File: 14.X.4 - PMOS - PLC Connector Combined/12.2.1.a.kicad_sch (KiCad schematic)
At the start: 65 parts, among them J301 Conn_01x01_PAD, J302 Conn_01x01_PAD, J303 Conn_01x01_PAD, J304 Conn_01x01_PAD, J305 Conn_01x01_PAD, J306 Conn_01x01_PAD, J307 Conn_01x01_PAD, J308 Conn_01x01_PAD, J309 Conn_01x01_PAD, J310 Conn_01x01_PAD, J311 Conn_01x01_PAD, J312 Conn_01x01_PAD, J313 Conn_01x01_PAD, J314 Conn_01x01_PAD, J315 Conn_01x01_PAD, J316 Conn_01x01_PAD, J317 DB128L-5.08-2P-BK-S, J318 DB128L-5.08-3P-BK-S, J319 DB128L-5.08-2P-BK-S, J320 DB128L-5.08-2P-BK-S, J321 B04B-XASK-1, Q1 2N7002, Q2 2N7002, Q3 2N7002, Q4 2N7002, U1 DMP6023LE-13, U2 DMP6023LE-13, U3 DMP6023LE-13, U4 DMP6023LE-13

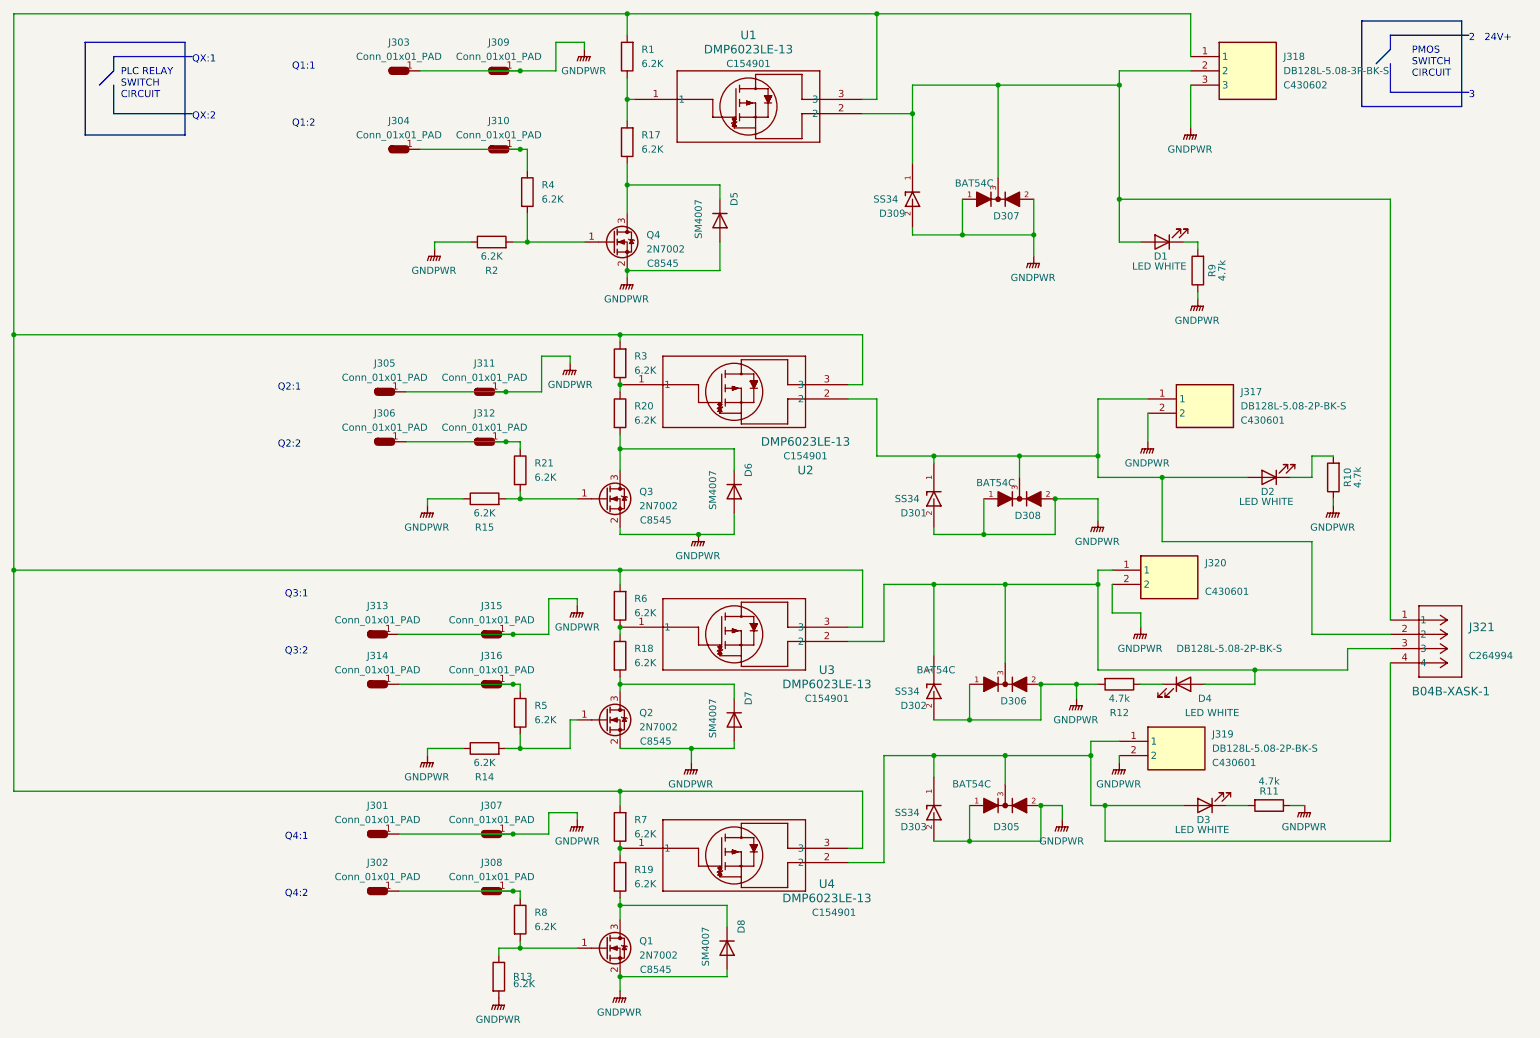
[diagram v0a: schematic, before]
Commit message: orientation of U1,U2,U3 and U4
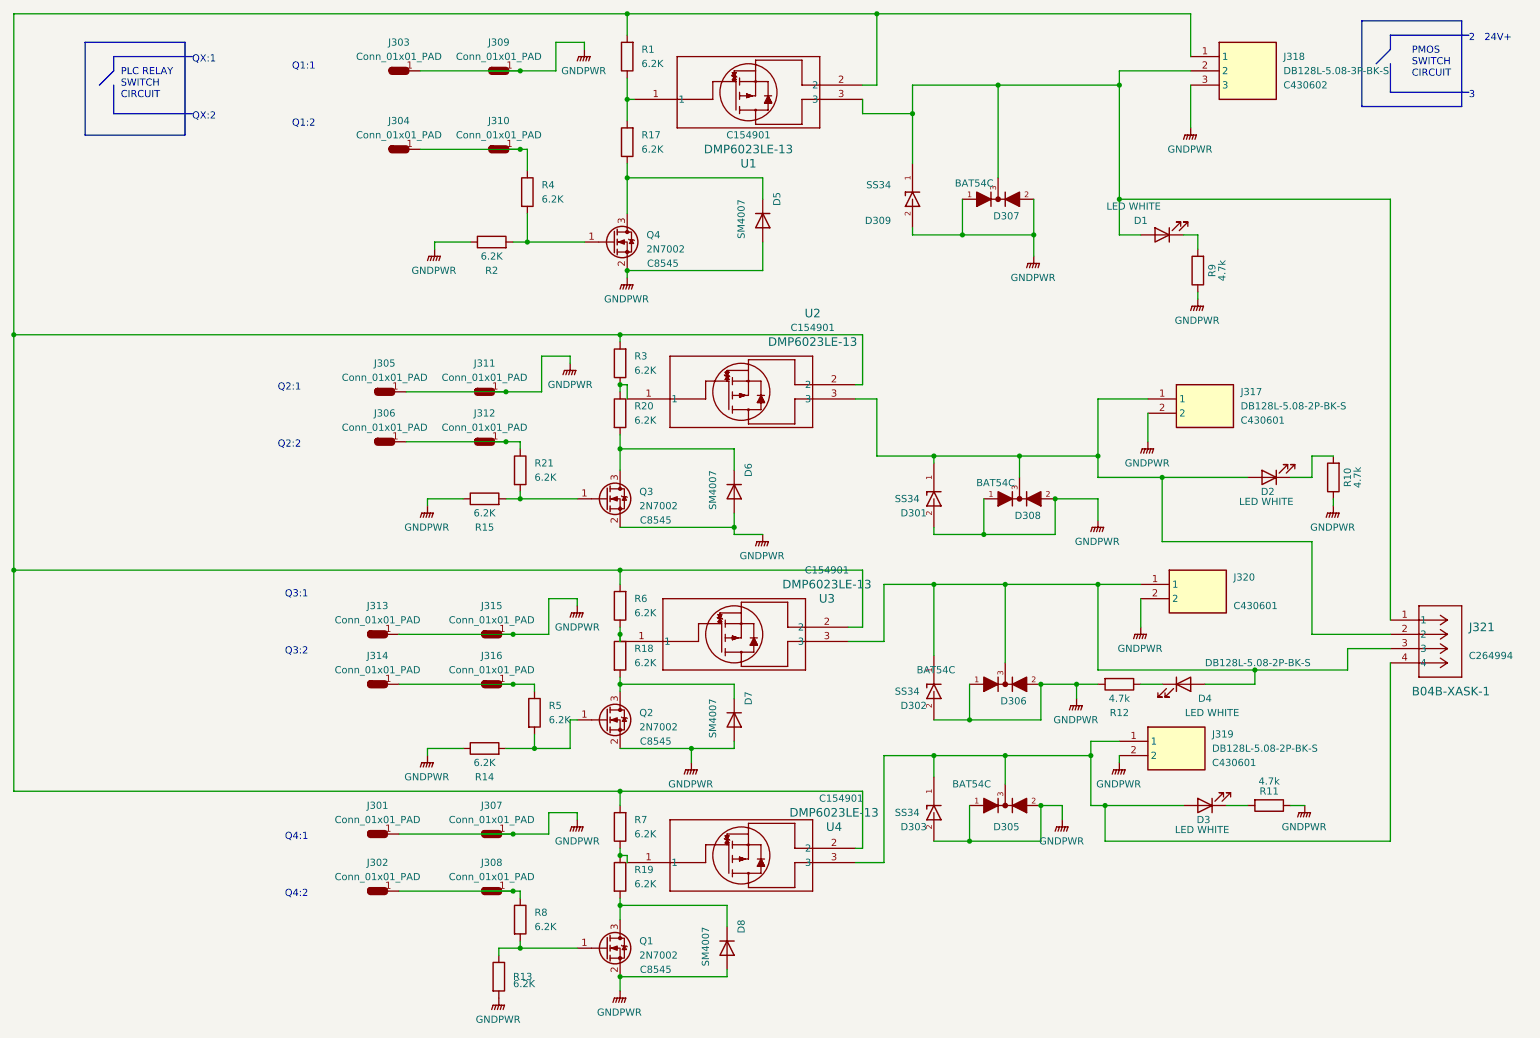
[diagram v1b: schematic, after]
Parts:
- J317: value DB128L-5.08-2P-BK-S -> DB128L-5.08-2P-BK-S
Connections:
- net at J318.1, R1.2, R3.2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: now also U1.2, U2.2, U3.2, U4.2; no longer U1.3, U2.3, U3.3, U4.3
- net at D1.2 (A), D307.3, D309.1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: now also U1.3; no longer U1.2
- net at D3.2 (A), D303.1, D305.3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: now also U4.3; no longer U4.2
- net at D302.1, D306.3, D4.2 (A)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: now also U3.3; no longer U3.2
- net at D2.2 (A), D301.1, D308.3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: now also U2.3; no longer U2.2
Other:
- moved on the sheet: D5, J320, U1, U2, U4
